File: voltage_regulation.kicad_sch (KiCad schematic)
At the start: 24 parts, among them IC8 NCV317BD2TR4G, U1 TPS73601MDRBREP, U2 TPS73601MDRBREP

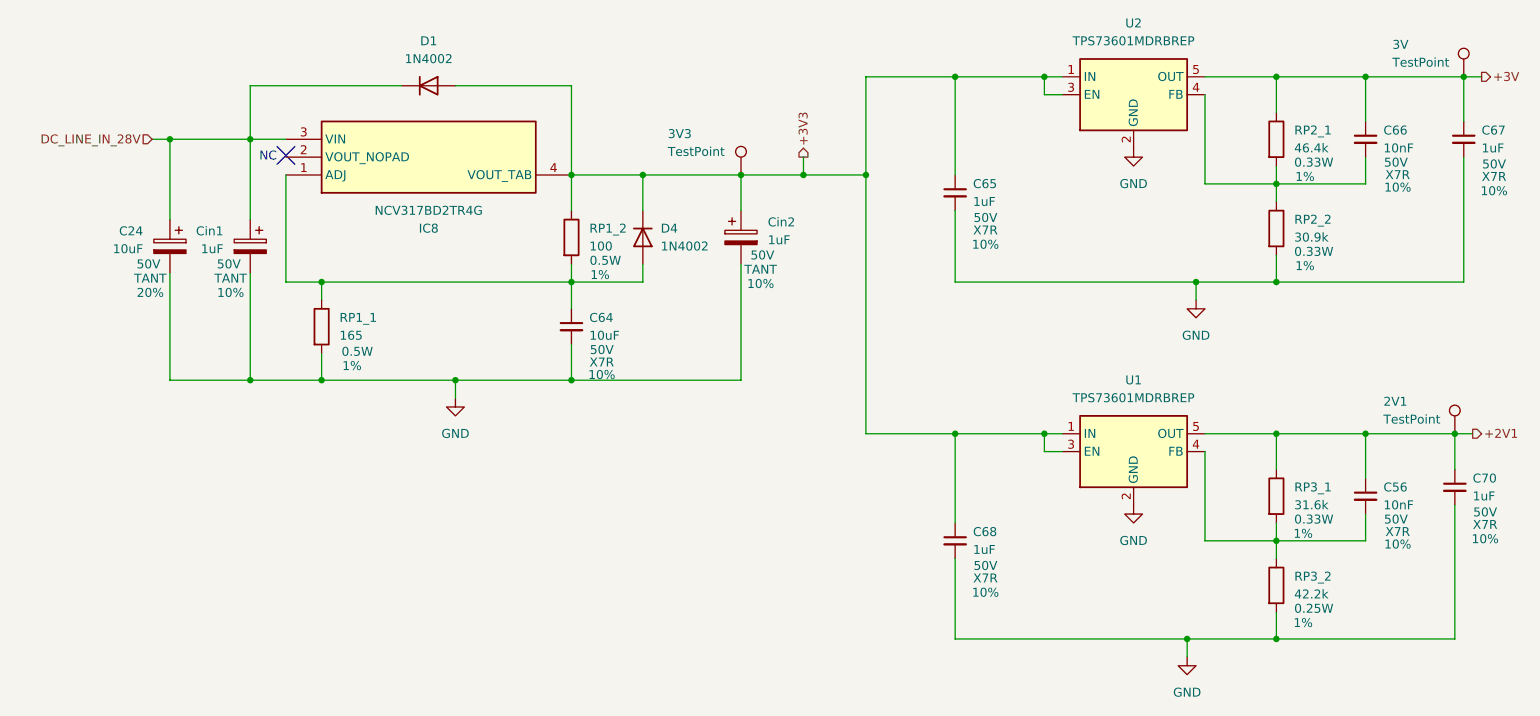
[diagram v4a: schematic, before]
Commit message: Ethernet Transceiver
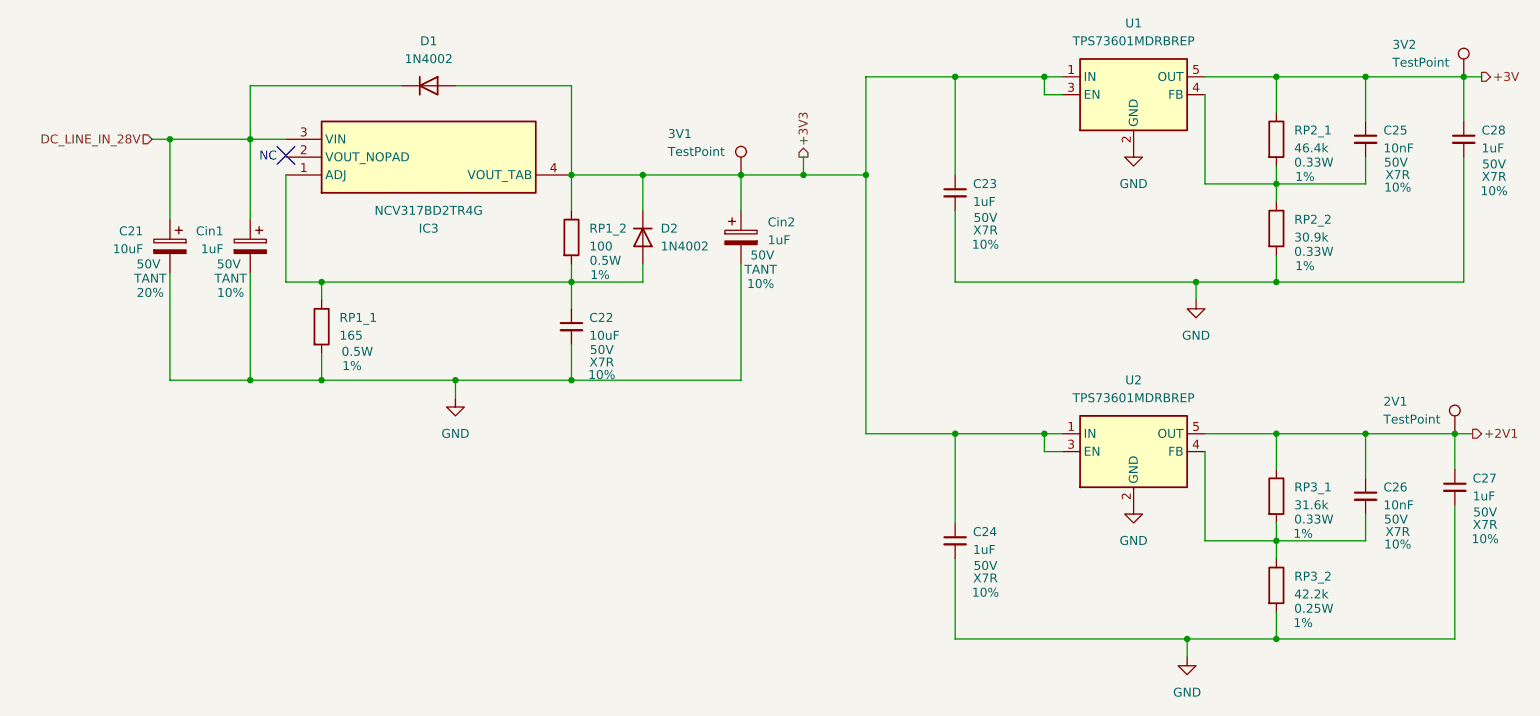
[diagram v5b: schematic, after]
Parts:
- renumbered 3V3 to 3V1, 3V to 3V2, C24 to C21, C64 to C22, C65 to C23, C68 to C24, C66 to C25, C56 to C26, C70 to C27, C67 to C28, D4 to D2, IC8 to IC3, U2 to U1, U1 to U2
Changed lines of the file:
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@@
 		(shape output)
 		(at 139.7 35.56 90)
-		(fields_autoplaced yes)
 		(effects
 			(font
@@
 		(shape output)
 		(at 236.22 24.13 0)
-		(fields_autoplaced yes)
 		(effects
 			(font
@@
 		(shape input)
 		(at 46.99 33.02 180)
-		(fields_autoplaced yes)
 		(effects
 			(font
@@
 		(shape output)
 		(at 234.95 74.93 0)
-		(fields_autoplaced yes)
 		(effects
 			(font
@@
 		(on_board yes)
 		(dnp no)
-		(property "Reference" "C56"
+		(property "Reference" "C26"
 			(at 222.25 82.5562 0)
 			(effects
@@
 			(project "S25-26"
 				(path "/6f4563ef-8a79-4567-b913-33c6dfb42b56/79b56aaa-8dda-4cfa-a280-62298a03532e"
-					(reference "C56")
+					(reference "C26")
 					(unit 1)
 				)
@@
 		(on_board yes)
 		(dnp no)
-		(property "Reference" "IC8"
+		(property "Reference" "IC3"
 			(at 86.36 45.72 0)
 			(effects
@@
 			(project "S25-26"
 				(path "/6f4563ef-8a79-4567-b913-33c6dfb42b56/79b56aaa-8dda-4cfa-a280-62298a03532e"
-					(reference "IC8")
+					(reference "IC3")
 					(unit 1)
 				)
@@
 		(dnp no)
 		(fields_autoplaced yes)
-		(property "Reference" "#PWR09"
+		(property "Reference" "#PWR028"
 			(at 186.69 40.64 0)
 			(effects
@@
 			(project "S25-26"
 				(path "/6f4563ef-8a79-4567-b913-33c6dfb42b56/79b56aaa-8dda-4cfa-a280-62298a03532e"
-					(reference "#PWR09")
+					(reference "#PWR028")
 					(unit 1)
 				)
@@
 		(dnp no)
 		(fields_autoplaced yes)
-		(property "Reference" "U1"
+		(property "Reference" "U2"
 			(at 186.69 67.31 0)
 			(effects
@@
 			(project "S25-26"
 				(path "/6f4563ef-8a79-4567-b913-33c6dfb42b56/79b56aaa-8dda-4cfa-a280-62298a03532e"
-					(reference "U1")
+					(reference "U2")
 					(unit 1)
 				)
@@
 		(dnp no)
 		(fields_autoplaced yes)
-		(property "Reference" "#PWR028"
+		(property "Reference" "#PWR031"
 			(at 195.58 62.23 0)
 			(effects
@@
 			(project "S25-26"
 				(path "/6f4563ef-8a79-4567-b913-33c6dfb42b56/79b56aaa-8dda-4cfa-a280-62298a03532e"
-					(reference "#PWR028")
+					(reference "#PWR031")
 					(unit 1)
 				)
@@
 		(on_board yes)
 		(dnp no)
-		(property "Reference" "C64"
+		(property "Reference" "C22"
 			(at 109.22 58.4262 0)
 			(effects
@@
 			(project ""
 				(path "/6f4563ef-8a79-4567-b913-33c6dfb42b56/79b56aaa-8dda-4cfa-a280-62298a03532e"
-					(reference "C64")
+					(reference "C22")
 					(unit 1)
 				)
@@
 		(on_board yes)
 		(dnp no)
-		(property "Reference" "C65"
+		(property "Reference" "C23"
 			(at 163.83 39.3762 0)
 			(effects
@@
 			(project "S25-26"
 				(path "/6f4563ef-8a79-4567-b913-33c6dfb42b56/79b56aaa-8dda-4cfa-a280-62298a03532e"
-					(reference "C65")
+					(reference "C23")
 					(unit 1)
 				)
@@
 		(on_board yes)
 		(dnp no)
-		(property "Reference" "C67"
+		(property "Reference" "C28"
 			(at 236.22 31.7562 0)
 			(effects
@@
 			(project "S25-26"
 				(path "/6f4563ef-8a79-4567-b913-33c6dfb42b56/79b56aaa-8dda-4cfa-a280-62298a03532e"
-					(reference "C67")
+					(reference "C28")
 					(unit 1)
 				)
@@
 		(dnp no)
 		(fields_autoplaced yes)
-		(property "Reference" "D4"
+		(property "Reference" "D2"
 			(at 119.38 45.7199 90)
 			(effects
@@
 			(project "S25-26"
 				(path "/6f4563ef-8a79-4567-b913-33c6dfb42b56/79b56aaa-8dda-4cfa-a280-62298a03532e"
-					(reference "D4")
+					(reference "D2")
 					(unit 1)
 				)
@@
 		(dnp no)
 		(fields_autoplaced yes)
-		(property "Reference" "U2"
+		(property "Reference" "U1"
 			(at 186.69 16.51 0)
 			(effects
@@
 			(project "S25-26"
 				(path "/6f4563ef-8a79-4567-b913-33c6dfb42b56/79b56aaa-8dda-4cfa-a280-62298a03532e"
-					(reference "U2")
+					(reference "U1")
 					(unit 1)
 				)
@@
 		(on_board yes)
 		(dnp no)
-		(property "Reference" "C68"
+		(property "Reference" "C24"
 			(at 163.83 88.9062 0)
 			(effects
@@
 			(project "S25-26"
 				(path "/6f4563ef-8a79-4567-b913-33c6dfb42b56/79b56aaa-8dda-4cfa-a280-62298a03532e"
-					(reference "C68")
+					(reference "C24")
 					(unit 1)
 				)
@@
 		(on_board yes)
 		(dnp no)
-		(property "Reference" "C70"
+		(property "Reference" "C27"
 			(at 234.95 81.2862 0)
 			(effects
@@
 			(project "S25-26"
 				(path "/6f4563ef-8a79-4567-b913-33c6dfb42b56/79b56aaa-8dda-4cfa-a280-62298a03532e"
-					(reference "C70")
+					(reference "C27")
 					(unit 1)
 				)
@@
 		(on_board yes)
 		(dnp no)
-		(property "Reference" "3V3"
+		(property "Reference" "3V1"
 			(at 120.396 32.258 0)
 			(effects
@@
 			(project "S25-26"
 				(path "/6f4563ef-8a79-4567-b913-33c6dfb42b56/79b56aaa-8dda-4cfa-a280-62298a03532e"
-					(reference "3V3")
+					(reference "3V1")
 					(unit 1)
 				)
@@
 		(on_board yes)
 		(dnp no)
-		(property "Reference" "3V"
+		(property "Reference" "3V2"
 			(at 223.52 19.558 0)
 			(effects
@@
 			(project "S25-26"
 				(path "/6f4563ef-8a79-4567-b913-33c6dfb42b56/79b56aaa-8dda-4cfa-a280-62298a03532e"
-					(reference "3V")
+					(reference "3V2")
 					(unit 1)
 				)
@@
 		(dnp no)
 		(fields_autoplaced yes)
-		(property "Reference" "#PWR010"
+		(property "Reference" "#PWR029"
 			(at 186.69 91.44 0)
 			(effects
@@
 			(project "S25-26"
 				(path "/6f4563ef-8a79-4567-b913-33c6dfb42b56/79b56aaa-8dda-4cfa-a280-62298a03532e"
-					(reference "#PWR010")
+					(reference "#PWR029")
 					(unit 1)
 				)
@@
 		(dnp no)
 		(fields_autoplaced yes)
-		(property "Reference" "#PWR029"
+		(property "Reference" "#PWR030"
 			(at 194.31 113.03 0)
 			(effects
@@
 			(project "S25-26"
 				(path "/6f4563ef-8a79-4567-b913-33c6dfb42b56/79b56aaa-8dda-4cfa-a280-62298a03532e"
-					(reference "#PWR029")
+					(reference "#PWR030")
 					(unit 1)
 				)
@@
 		(on_board yes)
 		(dnp no)
-		(property "Reference" "C24"
+		(property "Reference" "C21"
 			(at 45.72 46.1009 0)
 			(effects
@@
 			(project "S25-26"
 				(path "/6f4563ef-8a79-4567-b913-33c6dfb42b56/79b56aaa-8dda-4cfa-a280-62298a03532e"
-					(reference "C24")
+					(reference "C21")
 					(unit 1)
 				)
@@
 		(on_board yes)
 		(dnp no)
-		(property "Reference" "C66"
+		(property "Reference" "C25"
 			(at 222.25 31.7562 0)
 			(effects
@@
 			(project "S25-26"
 				(path "/6f4563ef-8a79-4567-b913-33c6dfb42b56/79b56aaa-8dda-4cfa-a280-62298a03532e"
-					(reference "C66")
-					(unit 1)
-				)
+					(reference "C25")
+					(unit 1)
+				)

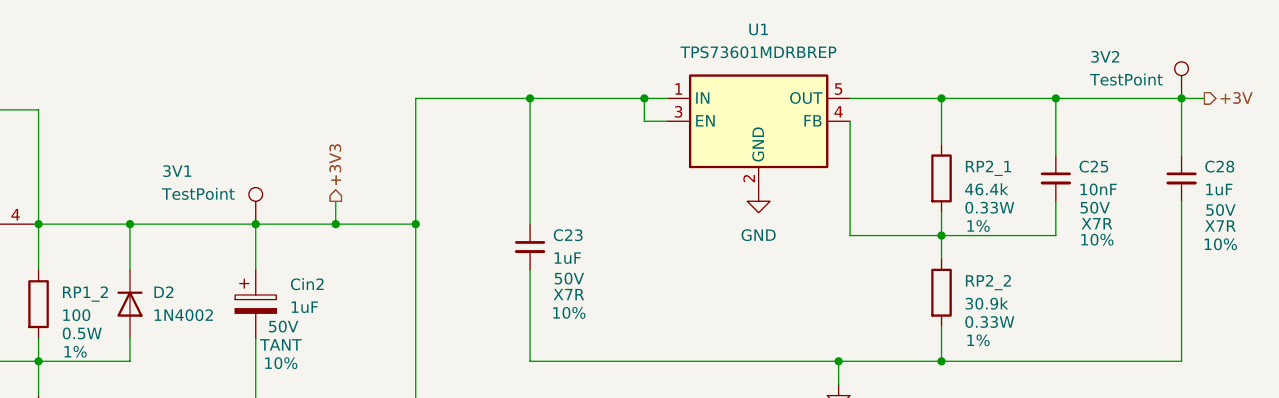
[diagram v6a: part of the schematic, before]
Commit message: Lots of PCB changes, some small parts changes
Updated parts footprints from those found in MDE Lab. Some parameters may be incorrect, but all footprints should be correct
Drew most of PCB. CMOS SPI still needs connection. Decoupling caps on MCU still need connection. Power and ground needs to be analyzed, and some components may not have power or ground connected.
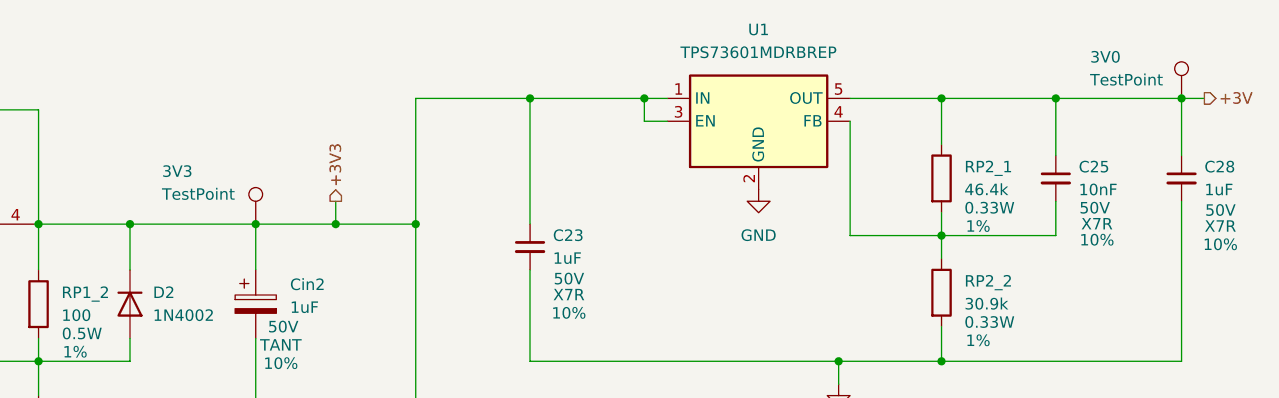
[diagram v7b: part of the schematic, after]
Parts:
- renumbered 3V2 to 3V0, 3V1 to 3V3
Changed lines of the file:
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@@
 		(on_board yes)
 		(dnp no)
-		(property "Reference" "3V1"
+		(property "Reference" "3V3"
 			(at 120.396 32.258 0)
 			(effects
@@
 			(project "S25-26"
 				(path "/6f4563ef-8a79-4567-b913-33c6dfb42b56/79b56aaa-8dda-4cfa-a280-62298a03532e"
-					(reference "3V1")
+					(reference "3V3")
 					(unit 1)
 				)
@@
 		(on_board yes)
 		(dnp no)
-		(property "Reference" "3V2"
+		(property "Reference" "3V0"
 			(at 223.52 19.558 0)
 			(effects
@@
 			(project "S25-26"
 				(path "/6f4563ef-8a79-4567-b913-33c6dfb42b56/79b56aaa-8dda-4cfa-a280-62298a03532e"
-					(reference "3V2")
+					(reference "3V0")
 					(unit 1)
 				)
